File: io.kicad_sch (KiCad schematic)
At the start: 55 parts, among them J1 Micro-Fit-12, Q1 NMOS 150V TBD, Q2 NMOS 150V TBD, U4 SIT1051AT/3

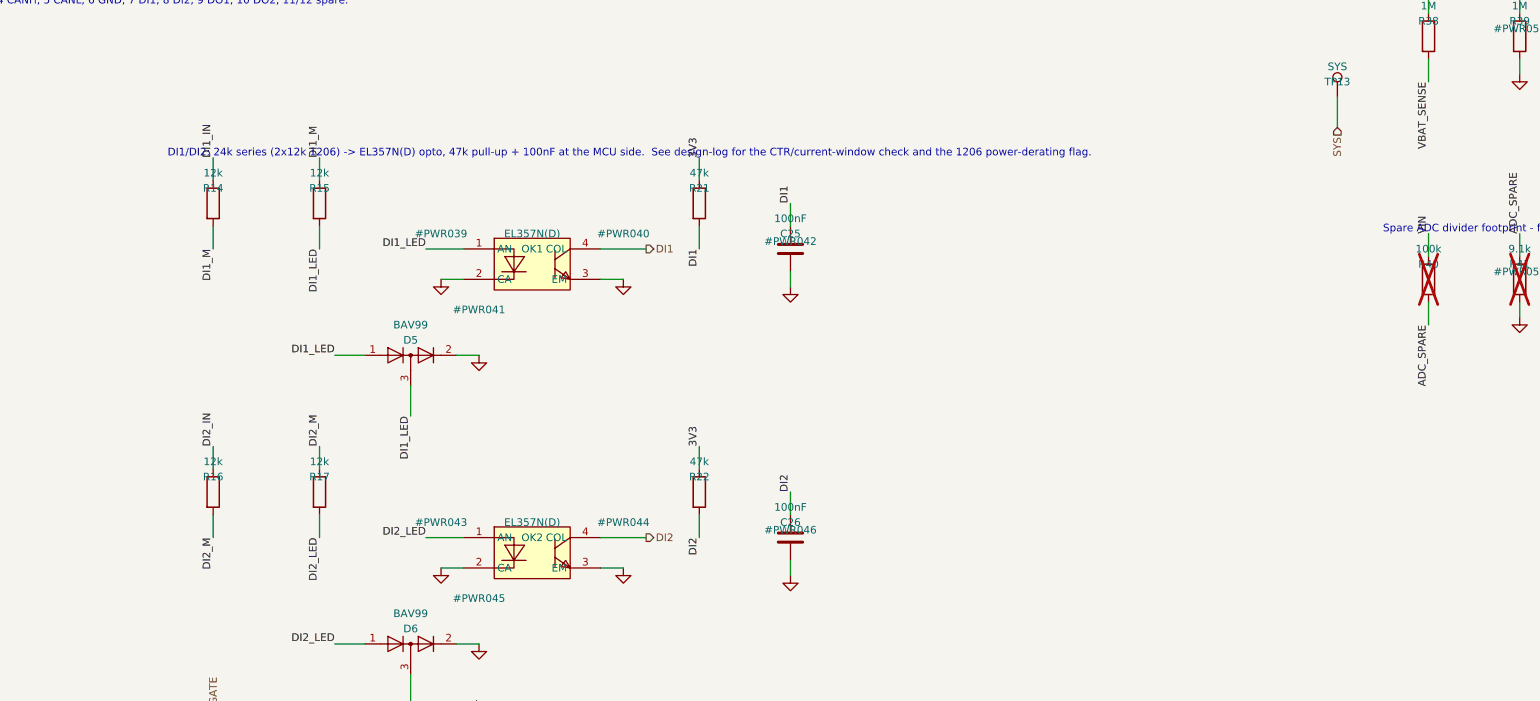
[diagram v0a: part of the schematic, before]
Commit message: M2: F-7 applied - DI series resistors 2x12k -> 3x12k
36k total per input. At 100 V each 12k 1206 now dissipates 0.090 W against
its ~0.125 W rating derated to 105 C ambient (72 % of rating), where two
resistors ran 0.204 W each (~1.6x over).

Current window at the new 10.5 V guaranteed floor: I_LED = 0.258 mA, giving
0.775 mA of collector drive at CTR >= 300 % against the 61.7 uA needed to
pull 3.3 V through 47 k below V_IL - 12.6x margin. At 100 V, I_LED = 2.74 mA.

Chain verified by netlist: J1.7 -> R14 -> R15 -> R16 -> DI1_LED, and
J1.8 -> R17 -> R18 -> R19 -> DI2_LED. ERC 0 errors.

Co-Authored-By: Claude Fable 5 <noreply@anthropic.com>
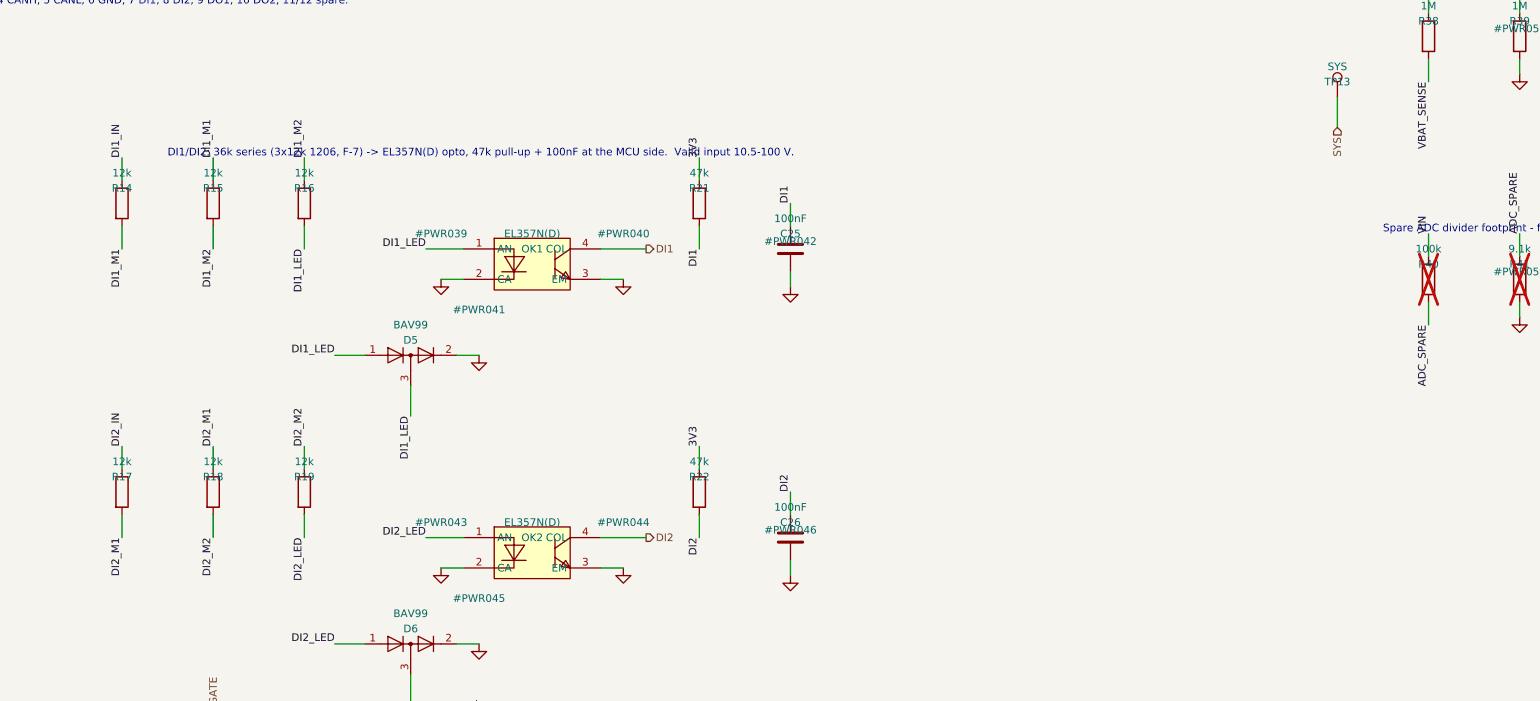
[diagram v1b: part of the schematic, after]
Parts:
- added R18, R19: 12k, Resistor_SMD:R_1206_3216Metric, symbol Device:R
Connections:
- net DI1_LED: now also R16.2; no longer R15.2
- net DI2_IN: now also R17.1; no longer R16.1
- net DI2_LED: now also R19.2; no longer R17.2
- net DI1_M renamed DI1_M1
- removed net DI2_M: R16.2, R17.1
- new net DI1_M2: R15.2, R16.1
- new net DI2_M1: R17.2, R18.1
- new net DI2_M2: R18.2, R19.1
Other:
- note added: "DI1/DI2: 36k series (3x12k 1206, F-7) -> EL357N(D) opto, 47k pull-up + 100nF at the MCU side. Valid input 10.5-100 V."
- note removed: "DI1/DI2: 24k series (2x12k 1206) -> EL357N(D) opto, 47k pull-up + 100nF at the MCU side. See design-log for the CTR/current-window check and the 1206 power-derating flag."
- moved on the sheet: R14, R15, R16, R17

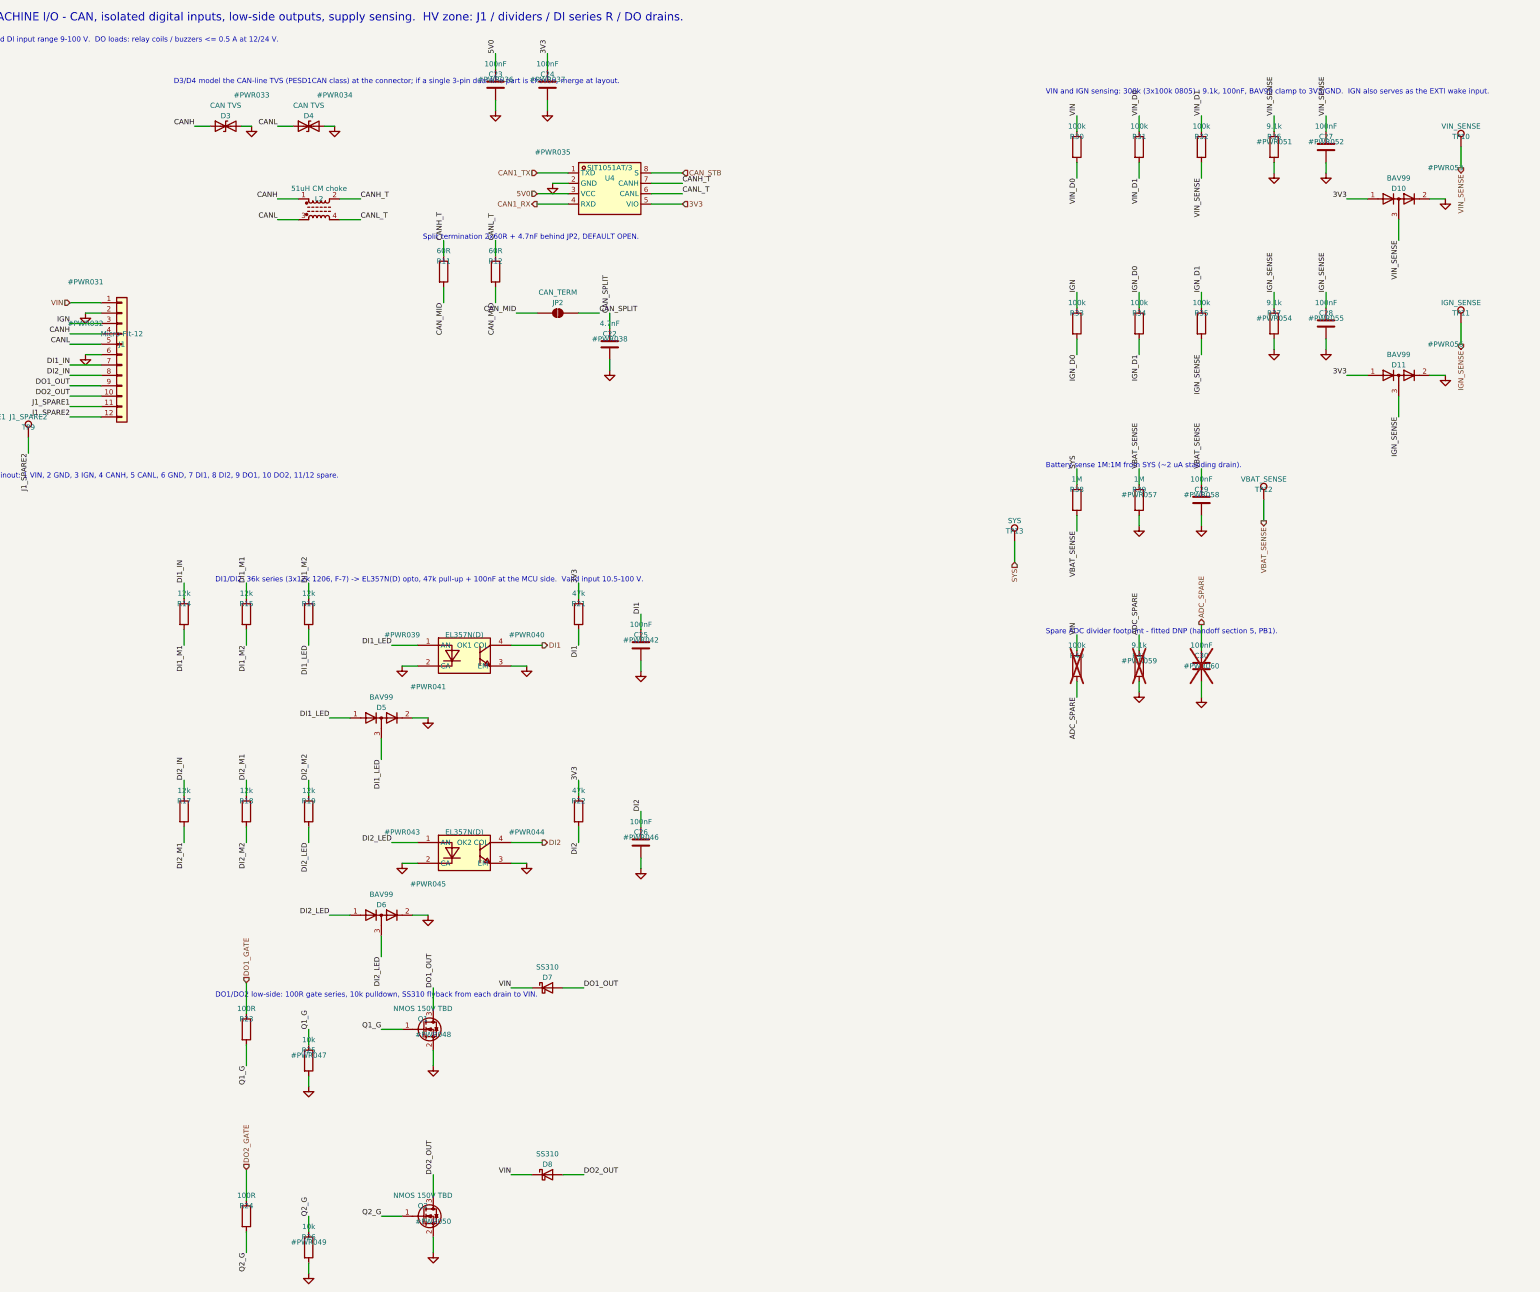
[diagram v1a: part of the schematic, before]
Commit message: M2: F-8 in-stock sweep complete - all TBD-F8 parts selected and wired
Selections (all datasheet- or API-verified, see design-log):
  Q1/Q2  AM2390N-TP 150V 4A SOT-23   C51886143 (F-10: gate drive caveat)
  D3     Nexperia PESD1CAN,215       C15771 (single dual-line part
         replaces the D3/D4 placeholder pair)
  L2     TDK ACT45B-510-2P-TL003     C76584 (windings 1->4 / 2->3 per TDK
         circuit diagram; alt clone C48928226 in Alternate field)
  J1     XUNPU WAFER-MX3.0-12PZZ     C7588012 (Molex 43045 stock footprint)
  D5/6/10/11 BAV99 Nexperia          C2500
  D7/D8  SS310 MDD                   C15874 (F-11: SS3200 C65001 recommended)
  R11/12 60.4R 1% YAGEO              C228935
  DI 12k 1206                        C17912
  47k / 100k / 9.1k / 1M 0805        C17713 / C17407 / C17855 / C17514
  C22    4.7nF X7R Samsung           C1621
D2 upgraded to Littelfuse SMDJ100A   C1977839 (per U5 approval condition b)

Generator: third silent-merge failure mode found and guarded -
a label point landing mid-span on another net's wire segment. The guard
caught D3's CANL label sitting on L2's CANH stub (KiCad had reported it
only as a multiple_net_names warning). CAN pair verified by netlist:
CANH = J1.4+D3.1+L2.1, CANH_T = L2.4+R11+U4.7, same for CANL via 2->3.

ERC 0 errors.

Co-Authored-By: Claude Fable 5 <noreply@anthropic.com>
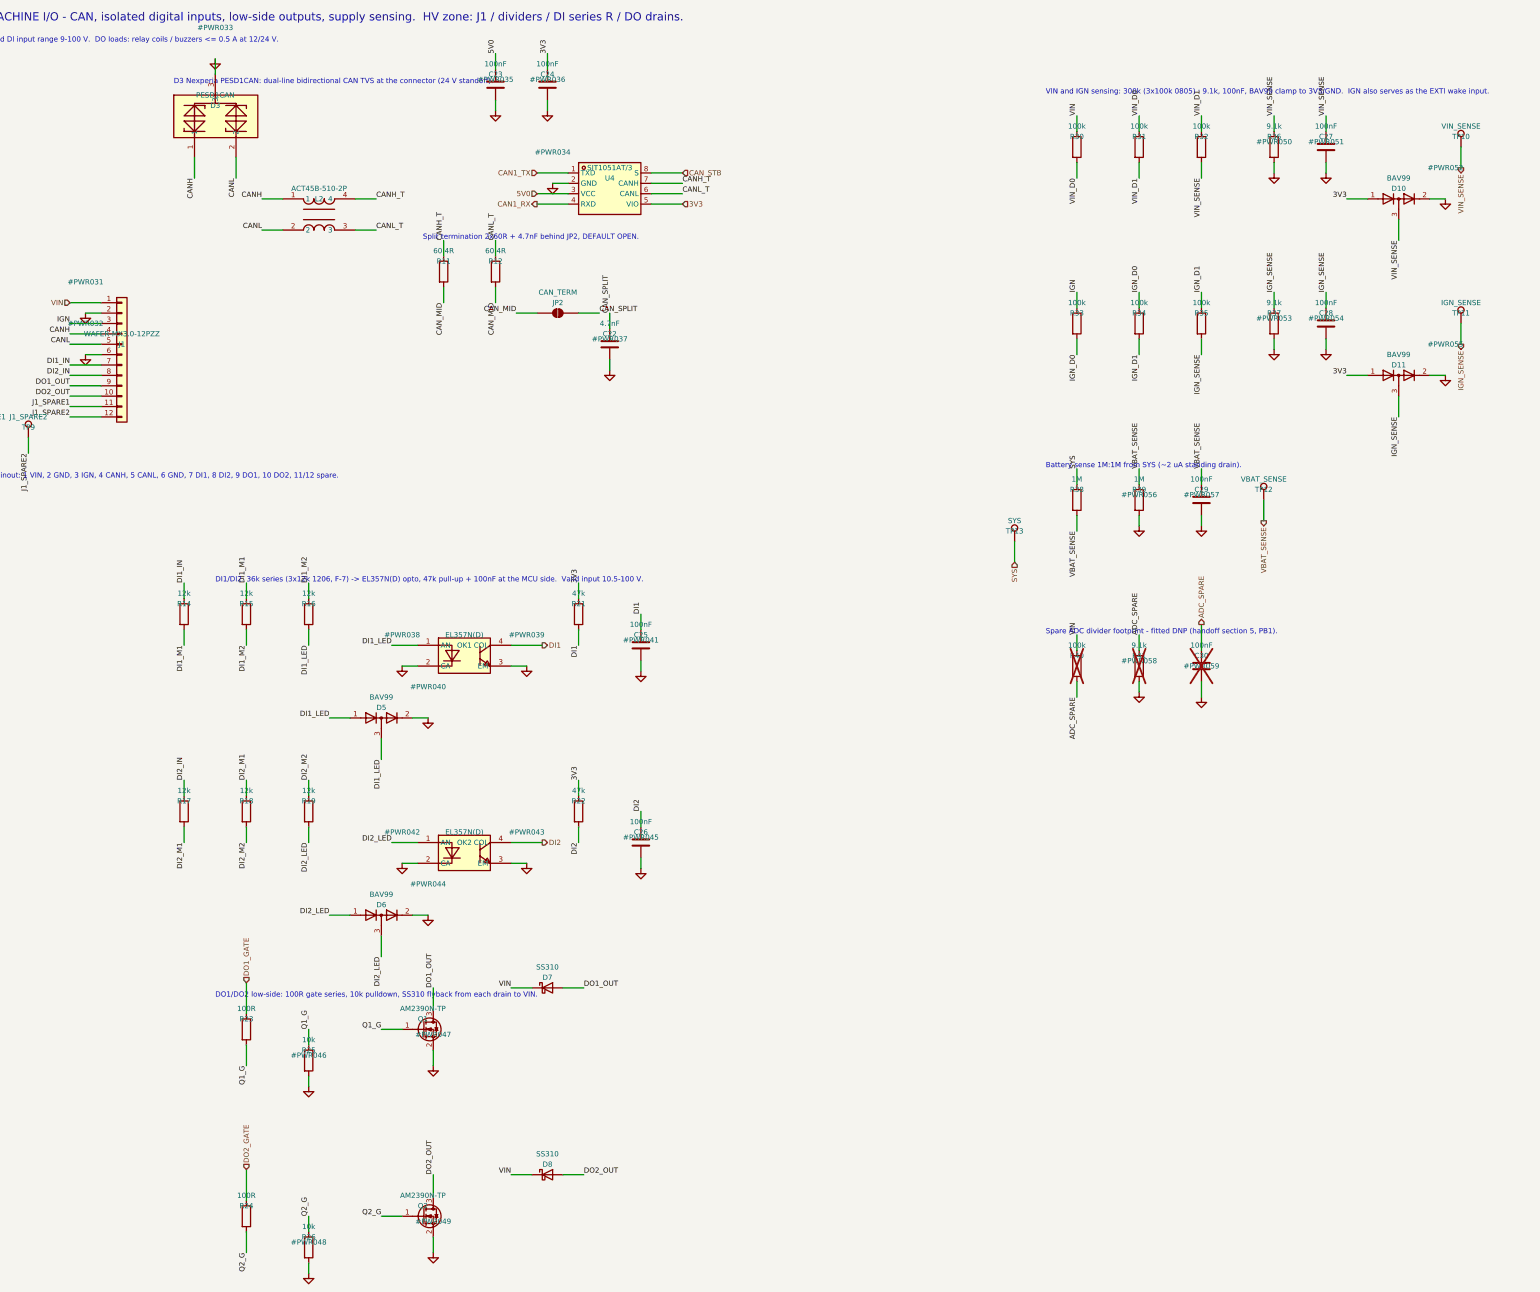
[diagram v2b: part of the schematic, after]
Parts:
- removed D4: CAN TVS, TBD:CAN_TVS, symbol Device:D_TVS
- C22: LCSC TBD-F8 -> C1621
- D10, D11, D5, D6: LCSC TBD-F8 -> C2500
- D3: value CAN TVS -> PESD1CAN; footprint TBD:CAN_TVS -> jlc:SOT-23_L2.9-W1.3-P1.90-LS2.4-BR; symbol Device:D_TVS -> jlc:PESD1CAN,215; LCSC TBD-F8 -> C15771
- D7, D8: LCSC TBD-F8 -> C15874
- J1: value Micro-Fit-12 -> WAFER-MX3.0-12PZZ; footprint TBD:MicroFit3_12pin -> Connector_Molex:Molex_Micro-Fit_3.0_43045-1212_2x06_P3.00mm_Vertical; LCSC TBD-F8 -> C7588012
- L2: value 51uH CM choke -> ACT45B-510-2P; footprint TBD:CM_choke_4pin -> jlc:IND-SMD_4P-L4.5-W3.2-TL; symbol Device:L_Ferrite_Coupled -> jlc:ACT45B-510-2P-TL003; Alternate (none) -> MetalLions ACT45B-510-2P-TF C48928226; LCSC TBD-F8 -> C76584
- Q1, Q2: value NMOS 150V TBD -> AM2390N-TP; footprint Package_TO_SOT_SMD:SOT-23 -> jlc:SOT-23-3_L2.9-W1.3-P1.90-LS2.4-BR; LCSC TBD-F8 -> C51886143
- R11, R12: value 60R -> 60.4R; LCSC TBD-F8 -> C228935
- R14, R15, R16, R17, R18, R19: LCSC TBD-F8 -> C17912
- R21, R22: LCSC TBD-F8 -> C17713
- R23, R24: LCSC TBD-F8 -> C17408
- R30, R31, R32, R33, R34, R35, R40: LCSC TBD-F8 -> C17407
- R36, R37, R41: LCSC TBD-F8 -> C17855
- R38, R39: LCSC TBD-F8 -> C17514
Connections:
- net CANH_T: now also L2.4; no longer L2.2
- net CANL: now also D3.2, L2.2; no longer L2.3
- net CANL_T: now also L2.3; no longer L2.4
- net GND: now also D3.3; no longer D3.2 (A2)
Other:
- note added: "D3 Nexperia PESD1CAN: dual-line bidirectional CAN TVS at the connector (24 V standoff)."
- note removed: "D3/D4 model the CAN-line TVS (PESD1CAN class) at the connector; if a single 3-pin dual-line part is chosen, merge at layout."
